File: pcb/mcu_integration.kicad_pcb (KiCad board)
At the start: 4 copper layers, 100 x 100 mm, 104 parts, among them IC1 TL7660IDGKR, IC10 AD844_OPAMP_MEL, IC2 TL081IDT, IC3 FOD814_OPTO_NOSHD, IC4 UA78M33CDCYG3, IC5 FOD814_OPTO_MEL, IC6 AD844_OPAMP_AL, IC7 FOD814_OPTO_AL, IC8 AD844_OPAMP_NOSHD, J1 Micro_SD_Card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

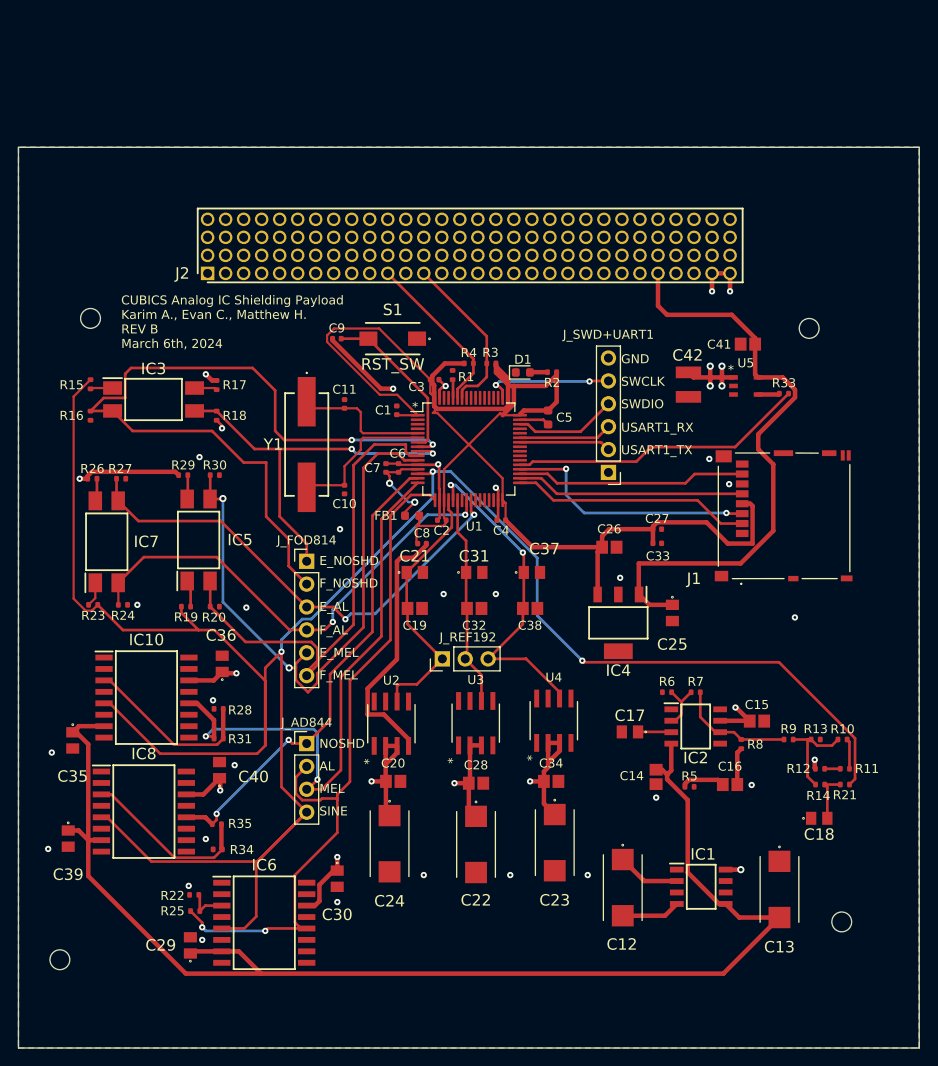
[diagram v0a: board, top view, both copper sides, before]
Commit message: TL766 footprint fixed
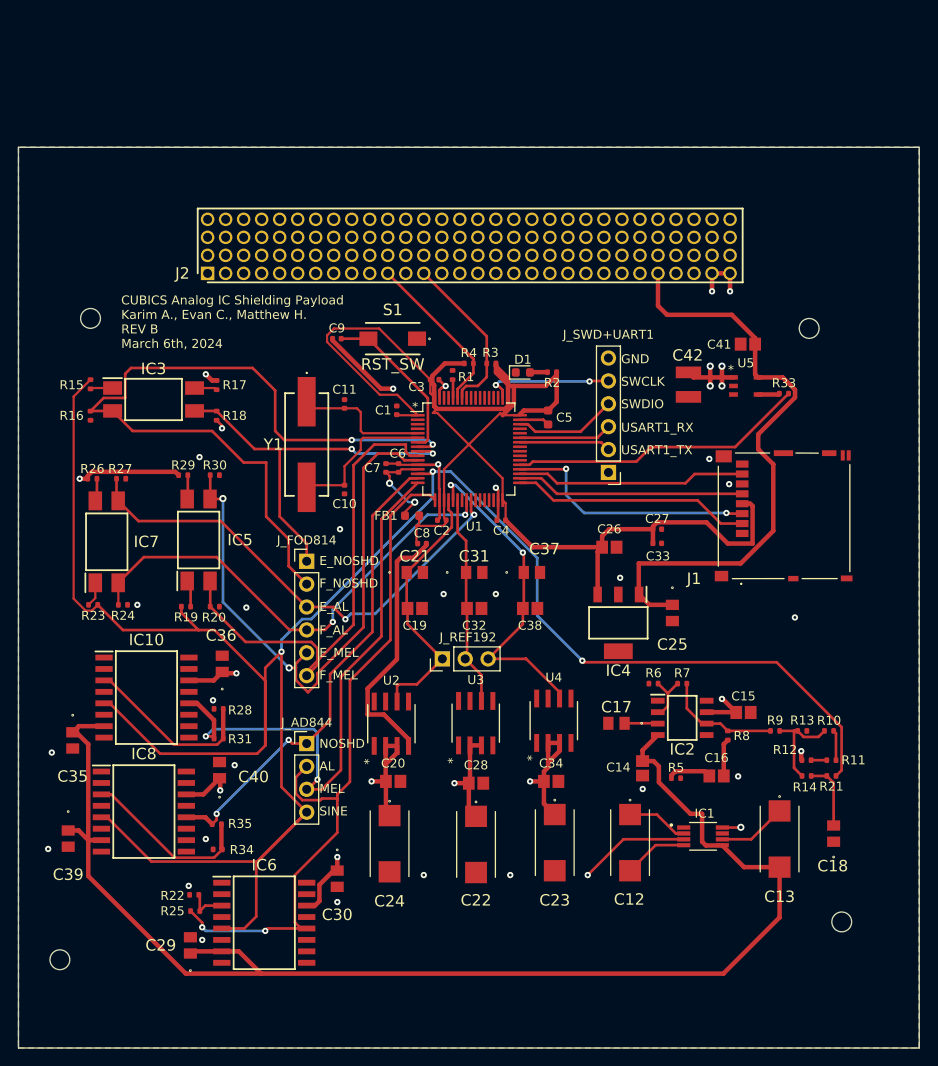
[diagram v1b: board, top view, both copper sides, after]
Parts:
- IC1: footprint capstone:SOIC127P600X175-8N -> capstone:SOP65P490X110-8N-actual
- moved IC1 5.60 mm to (159.0, 133.5)
- moved C13 5.60 mm to (167.5, 133.8)
- moved C12 5.06 mm to (150.9, 134.2)
- moved C18 2.33 mm to (173.5, 133.2), turned to 90 degrees
- moved C14 1.78 mm to (152.3, 125.9)
- moved C17 1.78 mm to (149.4, 120.9)
- moved R10 1.78 mm to (173.0, 121.8)
- moved R12 1.78 mm to (170.5, 125.0)
- moved C15 1.78 mm to (163.5, 119.7)
- moved C16 1.78 mm to (160.5, 126.8)
- moved IC2 1.78 mm to (156.7, 120.3)
- moved R11 1.78 mm to (173.3, 125.0)
- moved R13 1.78 mm to (170.0, 121.8)
- moved R14 1.78 mm to (170.5, 126.8)
- moved R21 1.78 mm to (173.3, 126.8)
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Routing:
- net GND: track 67.4 -> 87.3 mm
- net -5V Output: track 146.7 -> 149.7 mm
- net Net-(C18-Pad2): track 5.60 -> 7.55 mm
- net ADC1_IN0_SINE: track 255.0 -> 253.2 mm
- net Net-(C12--): track 6.54 -> 7.13 mm

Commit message: proper holes added
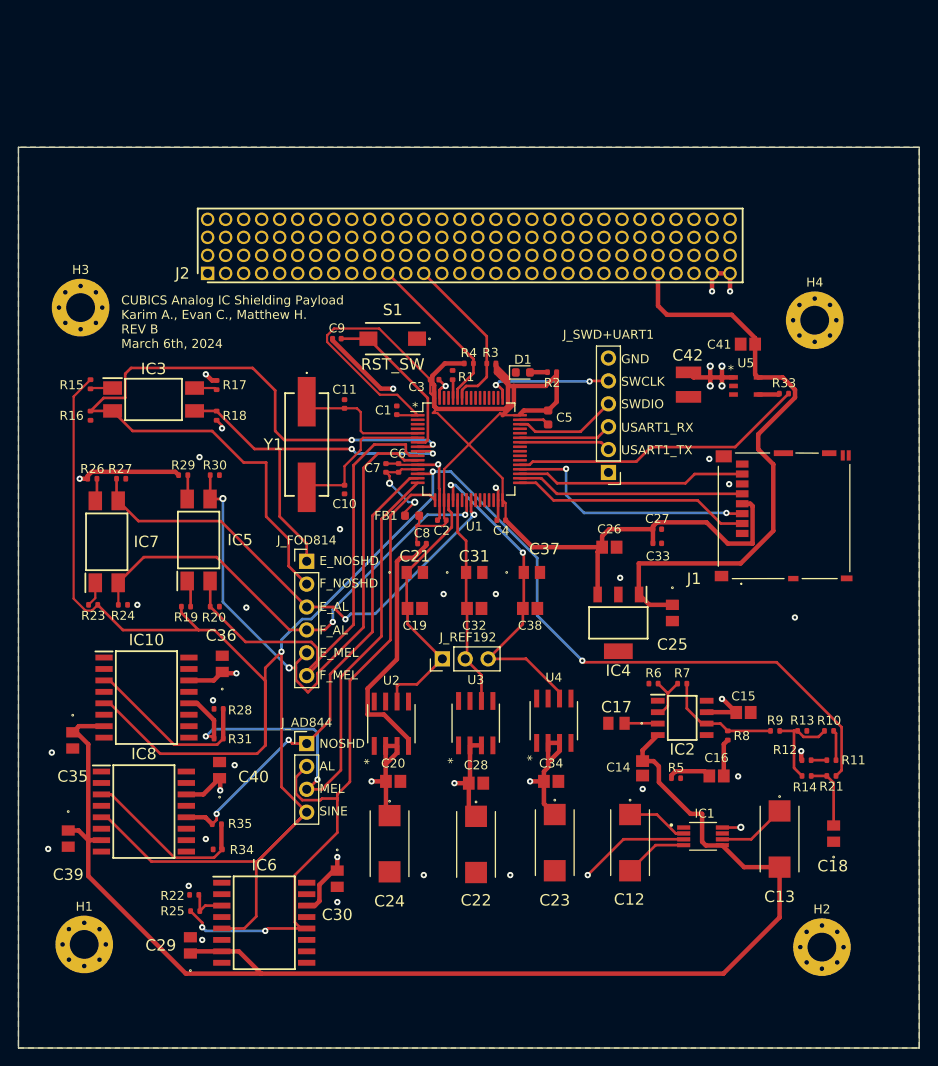
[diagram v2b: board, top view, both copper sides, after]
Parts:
- H1, H2, H3, H4: value MountingHole -> MountingHole_Pad; footprint MountingHole:MountingHole_2.2mm_M2 -> MountingHole:MountingHole_3.2mm_M3_Pad_Via
- moved H2 3.56 mm to (172.2, 145.8)
- moved H1 3.19 mm to (90.3, 145.5)
- moved H3 1.63 mm to (89.9, 74.8)
- moved H4 1.10 mm to (171.4, 76.2)

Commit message: hole sizing done, evan cap fix
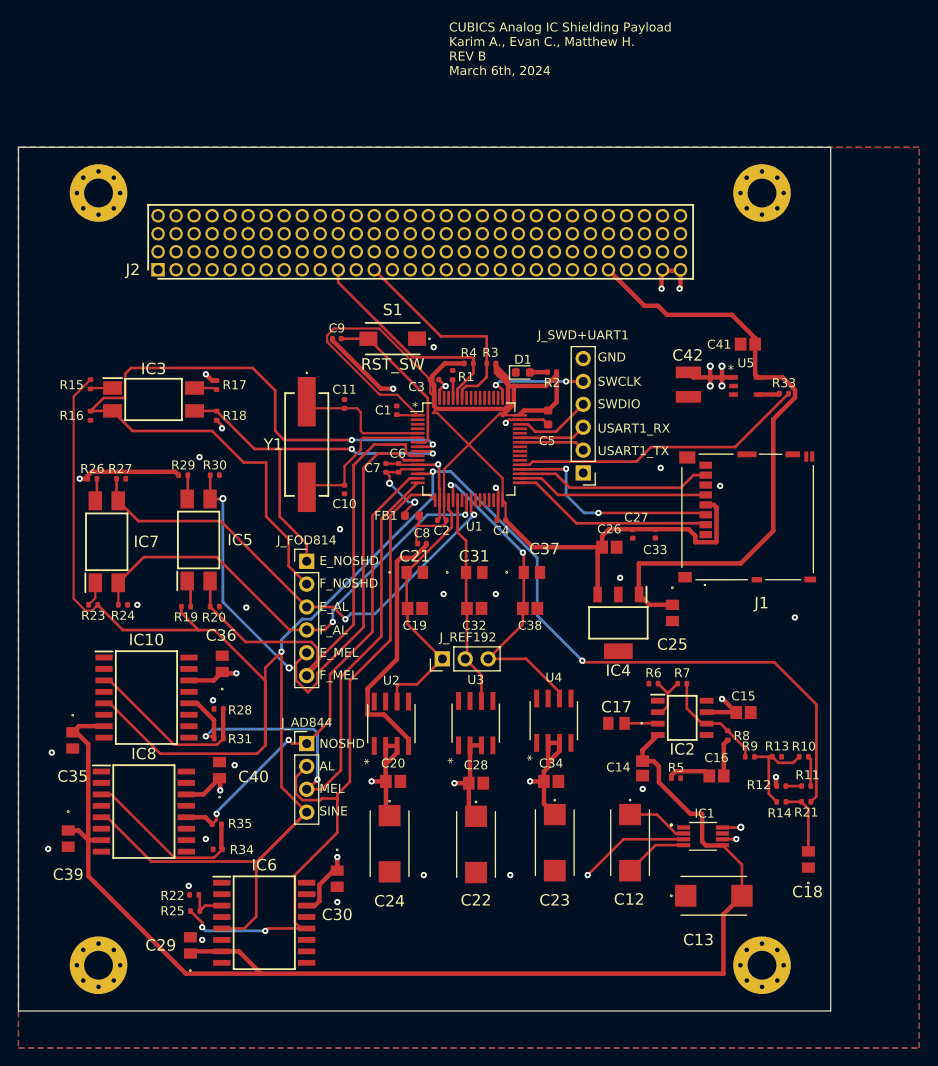
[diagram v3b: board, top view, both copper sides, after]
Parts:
- C16: value 0.1u -> 0.01u
- moved H4 15.3 mm to (165.6, 62.1)
- moved H3 12.9 mm to (91.9, 62.1)
- moved C13 9.64 mm to (160.2, 140.1), turned to 0 degrees
- moved H2 6.95 mm to (165.6, 147.8)
- moved J2 5.51 mm to (98.5, 70.6)
- moved J1 4.05 mm to (163.9, 96.1)
- moved C18 4.01 mm to (170.7, 136.1)
- moved R11 4.01 mm to (170.5, 127.9)
- moved R13 4.01 mm to (167.2, 124.7)
- moved R14 4.01 mm to (167.7, 129.7)
- moved R21 4.01 mm to (170.5, 129.7)
- moved R9 4.01 mm to (164.2, 124.7)
- moved R10 4.01 mm to (170.2, 124.7)
- moved R12 4.01 mm to (167.7, 127.9)
- moved H1 2.80 mm to (91.9, 147.8)
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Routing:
- net OBC_I2C_SDA: track 18.5 -> 25.0 mm
- net 3.3V Output: track 160.5 -> 154.2 mm
- net -5V Output: track 149.7 -> 144.0 mm
- net OBC_I2C_SCL: track 18.6 -> 24.3 mm
- net GND: track 87.3 -> 83.1 mm, vias 30 -> 32
- net /SPI2_MOSI: track 28.5 -> 24.3 mm
- net /SPI2_SCK: track 25.4 -> 21.4 mm
- net /SPI2_CS_NSS: track 26.5 -> 22.6 mm
- net /SPI2_MISO: track 25.5 -> 21.8 mm
- net /USART1_RX: track 10.3 -> 7.51 mm
- net /SWDIO: track 11.4 -> 8.62 mm
- net /USART1_TX: track 10.2 -> 7.39 mm
- net /SWCLK: track 14.5 -> 11.8 mm
- net /Evan -5V and signal gen/+5V_EXT: track 67.2 -> 69.3 mm
- net ADC1_IN0_SINE: track 253.2 -> 254.8 mm
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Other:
- board size 100 x 100 mm -> 90.2 x 95.9 mm

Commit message: mcu square wave sine header, more space for ic's should be ready for order
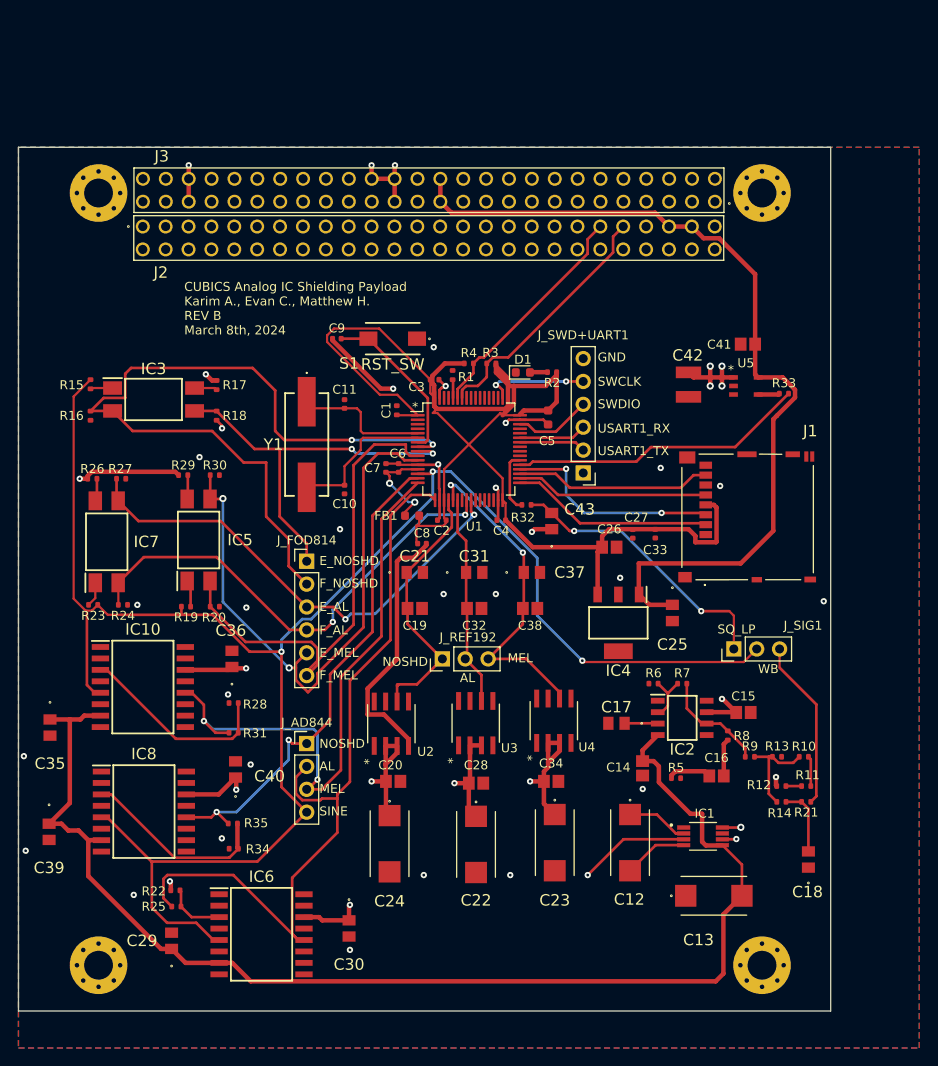
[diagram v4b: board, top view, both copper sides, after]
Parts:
- added C43: 0.01u, capstone:C0805, F.Cu at (142.2, 98.5)
- added J3: ESQ-126-39-L-D, capstone:ESQ-126-Y-X-D, F.Cu at (160.3, 63.0)
- added J_SIG1: Conn_01x03, Connector_PinHeader_2.54mm:PinHeader_1x03_P2.54mm_Vertical, F.Cu at (162.4, 112.7)
- added R32: 56k, Resistor_SMD:R_0402_1005Metric, F.Cu at (139.4, 96.7)
- C1: footprint Capacitor_SMD:C_0402_1005Metric -> Resistor_SMD:R_0402_1005Metric
- J2: value M22-6003005 -> ESQ-126-39-L-D; footprint capstone:RHDR120W55P200_4X30_6020X800X935P -> capstone:ESQ-126-Y-X-D
- moved C30 5.67 mm to (119.7, 143.7)
- moved J2 5.09 mm to (96.8, 65.8)
- moved C35 2.90 mm to (86.5, 121.4)
- moved C39 2.25 mm to (86.4, 133.0)
- moved R25 2.15 mm to (100.5, 141.3)
- moved R22 2.15 mm to (100.4, 139.5)
- moved C29 2.15 mm to (100.0, 145.1)
- moved R31 1.79 mm to (106.9, 122.0)
- moved R28 1.79 mm to (106.9, 118.7)
- moved R34 1.78 mm to (106.9, 134.9)
- moved R35 1.78 mm to (106.8, 132.1)
- moved C40 1.78 mm to (107.1, 126.1)
- moved IC6 1.31 mm to (110.0, 144.4)
- moved IC10 1.24 mm to (96.8, 116.9)
- moved C36 1.21 mm to (106.7, 113.8)
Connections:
- J2 pad 11: OBC_I2C_SDA -> unconnected-(J2-Pad11)
- J2 pad 13: OBC_I2C_SCL -> unconnected-(J2-Pad13)
- J2 pad 26: /Evan -5V and signal gen/+5V_EXT -> unconnected-(J2-Pad26)
- J2 pad 29: GND -> unconnected-(J2-Pad29)
- J2 pad 30: GND -> unconnected-(J2-Pad30)
- J2 pad 41: unconnected-(J2-Pad41) -> OBC_I2C_SDA
- J2 pad 43: unconnected-(J2-Pad43) -> OBC_I2C_SCL
- J2 pad 47: unconnected-(J2-Pad47) -> /Evan -5V and signal gen/+5V_EXT
- J2 pad 49: unconnected-(J2-Pad49) -> /Evan -5V and signal gen/+5V_EXT
- R21 pad 1: ADC1_IN0_SINE -> Net-(J_SIG1-Pin_3)
- U1 pad 38: unconnected-(U1-PC7-Pad38) -> SIG_SQUARE
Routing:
- net ADC1_IN0_SINE: track 254.8 -> 200.7 mm
- net Net-(J_SIG1-Pin_1): track 0.00 -> 31.3 mm, vias 0 -> 2
- net /Evan -5V and signal gen/+5V_EXT: track 69.3 -> 97.8 mm
- net Net-(J_SIG1-Pin_3): track 0.00 -> 18.9 mm
- net GND: track 83.1 -> 92.4 mm, vias 32 -> 34
- net ADC1_IN3_OPAMP_AL: track 80.0 -> 88.8 mm, vias 2 -> 0
- net SIG_SQUARE: track 0.00 -> 6.83 mm
- net OBC_I2C_SCL: track 24.3 -> 28.2 mm
- net -5V Output: track 144.0 -> 140.1 mm
- net +5V: track 90.3 -> 92.7 mm
- net Net-(IC10--IN): track 19.8 -> 22.0 mm
- net ADC1_IN1_OPAMP_NOSHD: track 53.3 -> 55.4 mm
- net Net-(IC6--IN): track 4.54 -> 6.57 mm
- net Net-(IC8--IN): track 19.6 -> 21.4 mm
- net ADC1_IN2_OPAMP_MEL: track 66.5 -> 67.9 mm
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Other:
- board text added: "CUBICS Analog IC Shielding Payload Karim A., Evan C., Matthew H. REV B March 8th, 2024"
- board text added: "SQ_LP"
- board text added: "WB"
- board text removed: "CUBICS Analog IC Shielding Payload Karim A., Evan C., Matthew H. REV B March 6th, 2024"

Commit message: ready for jlcpcb
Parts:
- moved R26 2.50 mm to (91.2, 91.3)
- moved R27 2.50 mm to (94.4, 91.3)
- moved R29 2.10 mm to (101.3, 91.3)
- moved R30 2.10 mm to (104.8, 91.3)
- moved C34 1.93 mm to (142.3, 129.3)
- moved C23 1.93 mm to (142.7, 136.1)
- moved C12 1.90 mm to (150.9, 136.1)
- moved C24 1.80 mm to (124.1, 136.1)
- moved C20 1.80 mm to (124.5, 129.2)
- moved C28 1.73 mm to (133.7, 129.3)
- moved C22 1.73 mm to (133.7, 136.1)
- moved IC7 1.30 mm to (92.8, 99.5)
- moved IC5 1.10 mm to (103.0, 99.5)
- moved U4 0.85 mm to (142.6, 121.5)
- moved U3 0.68 mm to (133.6, 121.6)
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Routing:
- net GND: track 92.4 -> 76.0 mm, vias 34 -> 35
- net ADC1_IN13_OPTO_E_MEL: track 66.6 -> 68.7 mm
- net ADC1_IN15_OPTO_E_AL: track 54.7 -> 56.4 mm
- net ADC1_IN12_OPTO_F_MEL: track 54.8 -> 53.3 mm
- net Net-(IC7-AK): track 2.76 -> 4.06 mm
- net Net-(IC7-C): track 2.52 -> 3.73 mm
- net Net-(IC5-AK): track 3.01 -> 4.11 mm
- net Net-(IC5-C): track 2.68 -> 3.68 mm
- net +5V: track 92.7 -> 91.8 mm
- net Net-(C12--): track 7.13 -> 7.92 mm
- net Net-(C12-+): track 6.82 -> 6.03 mm
- net ADC1_IN14_OPTO_F_AL: track 53.3 -> 54.1 mm
- net ADC1_IN6_VREF_AL: track 23.6 -> 24.2 mm
- net ADC1_IN4_VREF_NOSHD: track 29.7 -> 29.1 mm
- net Net-(IC10--IN): track 22.0 -> 22.6 mm
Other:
- board text added: "FORMAT AS FAT!"
- board text added: "NC"
- board text added: "https://github.com/kaitallaoua/capstone-pcb https://github.com/kaitallaoua/capstone-cubeide"
